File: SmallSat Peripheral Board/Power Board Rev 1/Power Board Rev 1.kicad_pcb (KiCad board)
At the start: 2 copper layers, 37 parts, among them U1 DMN3020UFDF, U2 BQ296202DSGR, U3 DMN3020UFDF, U4 BQ28Z620DRZR, U5 TPS62993QRYTRQ1, U6 TPS62993QRYTRQ1

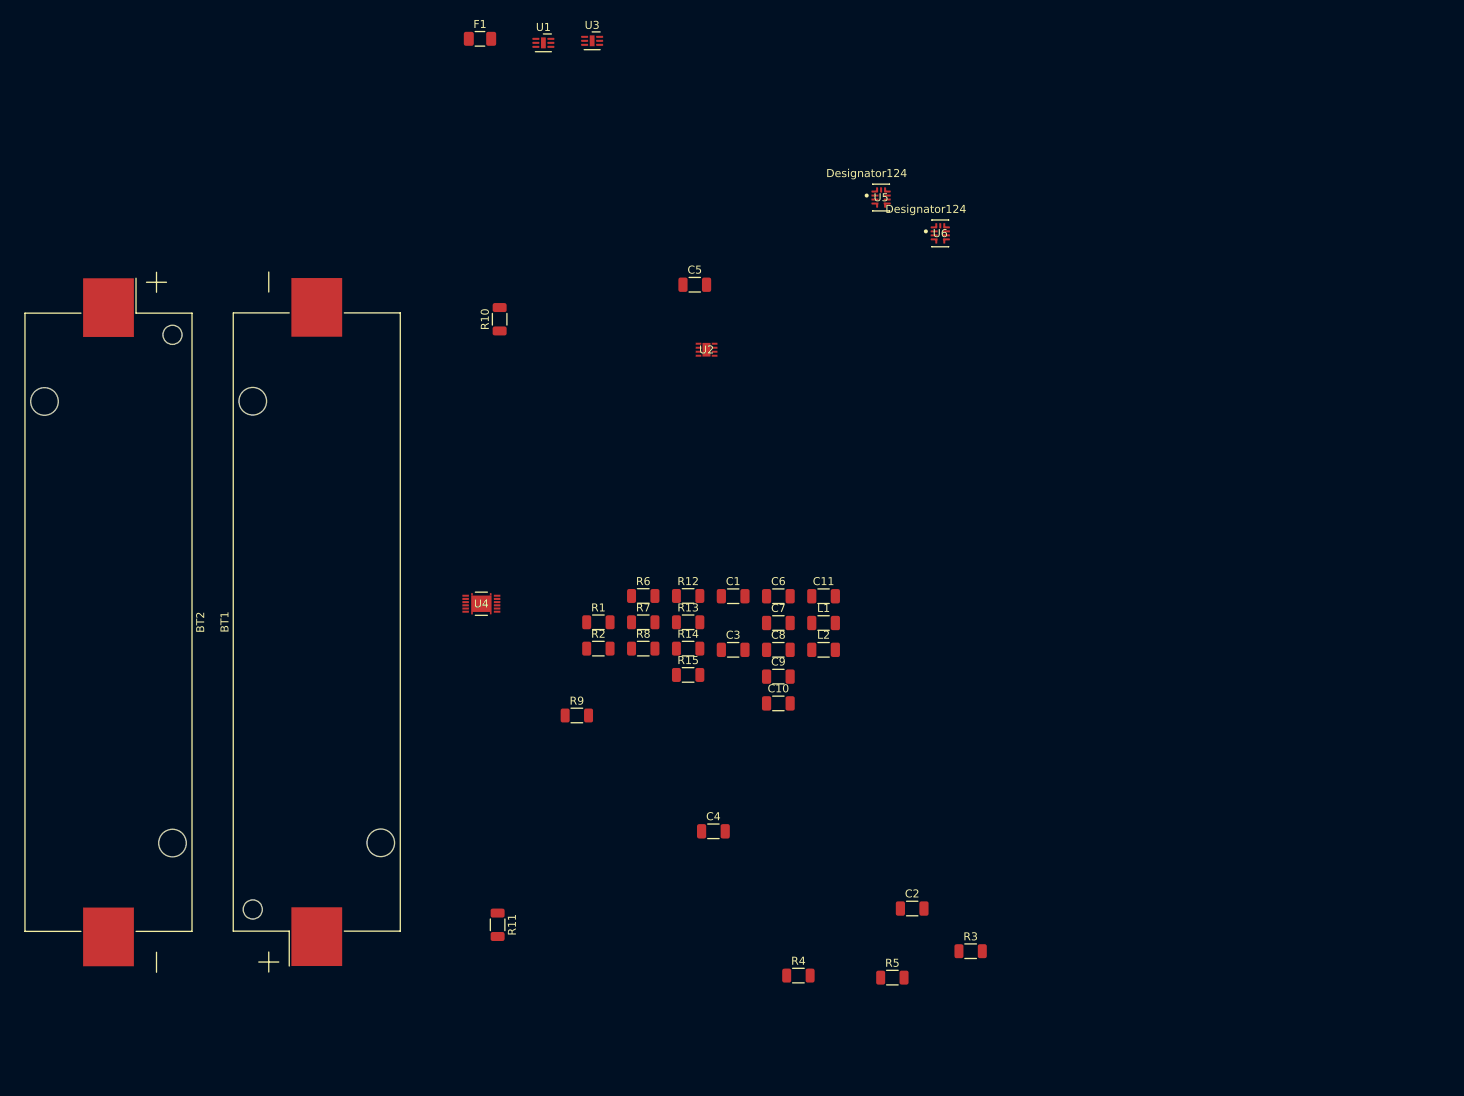
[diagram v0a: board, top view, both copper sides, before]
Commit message: Power Board Grouping
- Continuing to group parts
- Connectors figured out
- Filter circuit must be close to BQ298
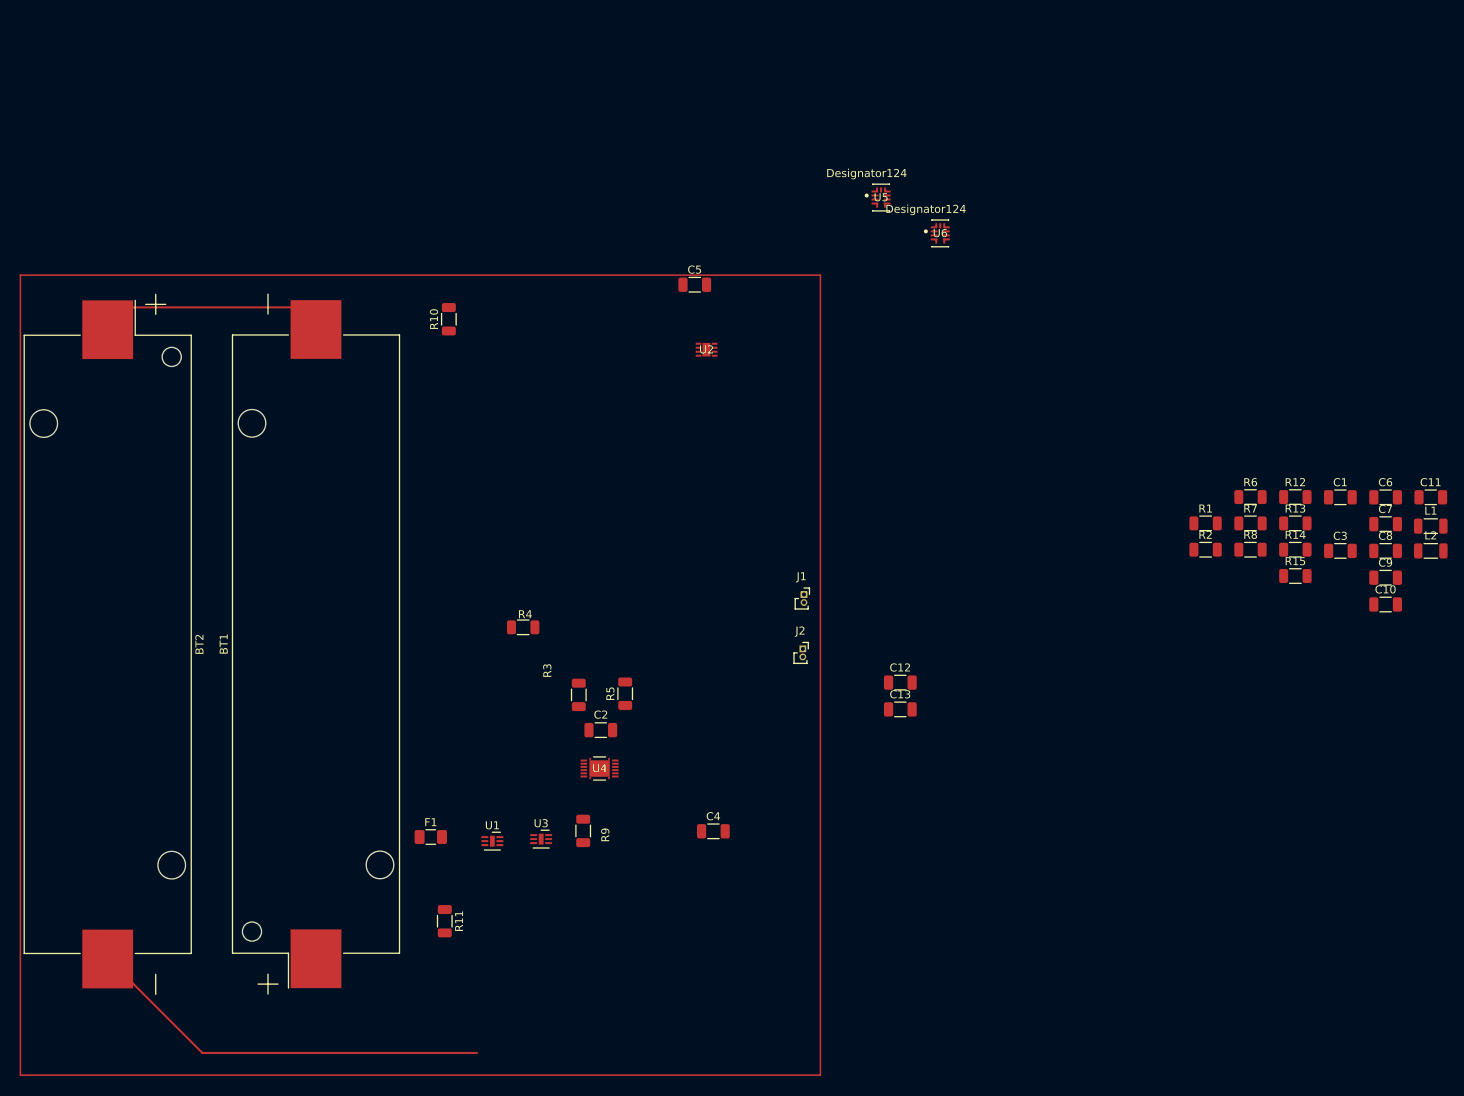
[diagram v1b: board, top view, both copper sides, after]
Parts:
- added C12: 0.1u, Capacitor_SMD:C_1206_3216Metric, F.Cu at (187.0, 108.4)
- added C13: 0.1u, Capacitor_SMD:C_1206_3216Metric, F.Cu at (187.0, 111.8)
- added J1: Conn_01x02_Pin, Connector_PinSocket_1.00mm:PinSocket_1x02_P1.00mm_Vertical, F.Cu at (174.9, 97.4)
- added J2: Conn_01x02_Pin, Connector_PinSocket_1.00mm:PinSocket_1x02_P1.00mm_Vertical, F.Cu at (174.8, 104.2)
- L1, L2: footprint Capacitor_SMD:C_1206_3216Metric -> Inductor_SMD:L_1206_3216Metric
- R3, R5: value 10m -> 100
- moved U1 100.0 mm to (136.0, 128.2)
- moved U3 100.0 mm to (142.1, 128.0)
- moved F1 100.0 mm to (128.3, 127.7)
- moved C1 76.9 mm to (242.0, 85.2)
- moved C10 76.9 mm to (247.7, 98.6)
- moved C11 76.9 mm to (253.3, 85.2)
- moved C3 76.9 mm to (242.0, 91.9)
- moved C6 76.9 mm to (247.7, 85.2)
- moved C7 76.9 mm to (247.7, 88.6)
- moved C8 76.9 mm to (247.7, 91.9)
- moved C9 76.9 mm to (247.7, 95.3)
- moved L2 76.9 mm to (253.3, 91.9)
- moved R1 76.9 mm to (225.2, 88.5)
- moved R12 76.9 mm to (236.4, 85.2)
- moved R13 76.9 mm to (236.4, 88.5)
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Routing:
- net GND: track 0.00 -> 54.1 mm
- net /B1+: track 0.00 -> 26.0 mm
- net /B2+: track 0.00 -> 6.14 mm

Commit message: Current Line Outline Complete
- OV/UV protection IC wired
- fuel gauge not wired
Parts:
- R2: value 1k -> 100
- moved R10 136.4 mm to (248.3, 131.8)
- moved C2 87.2 mm to (235.2, 131.2)
- moved C4 87.2 mm to (249.2, 143.8)
- moved R11 87.2 mm to (215.6, 155.1)
- moved R3 87.2 mm to (232.4, 126.8)
- moved R4 87.2 mm to (225.4, 118.3)
- moved R5 87.2 mm to (238.2, 126.7)
- moved R9 87.2 mm to (232.9, 143.8)
- moved L2 85.6 mm to (168.8, 105.0), turned to 180 degrees
- moved L1 84.8 mm to (169.0, 97.8), turned to 180 degrees
- moved R6 82.9 mm to (153.4, 115.0)
- moved C1 81.4 mm to (169.5, 122.3), turned to 90 degrees
- moved C3 75.3 mm to (173.1, 122.2), turned to -90 degrees
- moved R7 73.0 mm to (161.3, 111.0), turned to 90 degrees
- moved R2 72.8 mm to (163.6, 130.7), turned to -90 degrees
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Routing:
- net /B1+: track 26.0 -> 92.9 mm, vias 0 -> 2
- net /B2+: track 6.14 -> 61.0 mm
- net GND: track 54.1 -> 3.16 mm
- net /PACK+: track 0.00 -> 24.8 mm
- net Net-(U2-V1): track 0.00 -> 12.4 mm
- net Net-(U2-V2): track 0.00 -> 10.9 mm
- net Net-(U3-G): track 0.00 -> 10.6 mm, vias 0 -> 1
- net Net-(U1-D): track 0.00 -> 9.46 mm
- net /OUT: track 0.00 -> 7.42 mm
- net /BATT+: track 0.00 -> 6.65 mm
- net Net-(U2-VDD): track 0.00 -> 5.60 mm
- net /5V: track 0.00 -> 4.68 mm
- net /3.3V: track 0.00 -> 4.64 mm
- net Net-(U5-SW): track 0.00 -> 3.70 mm
- net Net-(U6-SW): track 0.00 -> 3.54 mm

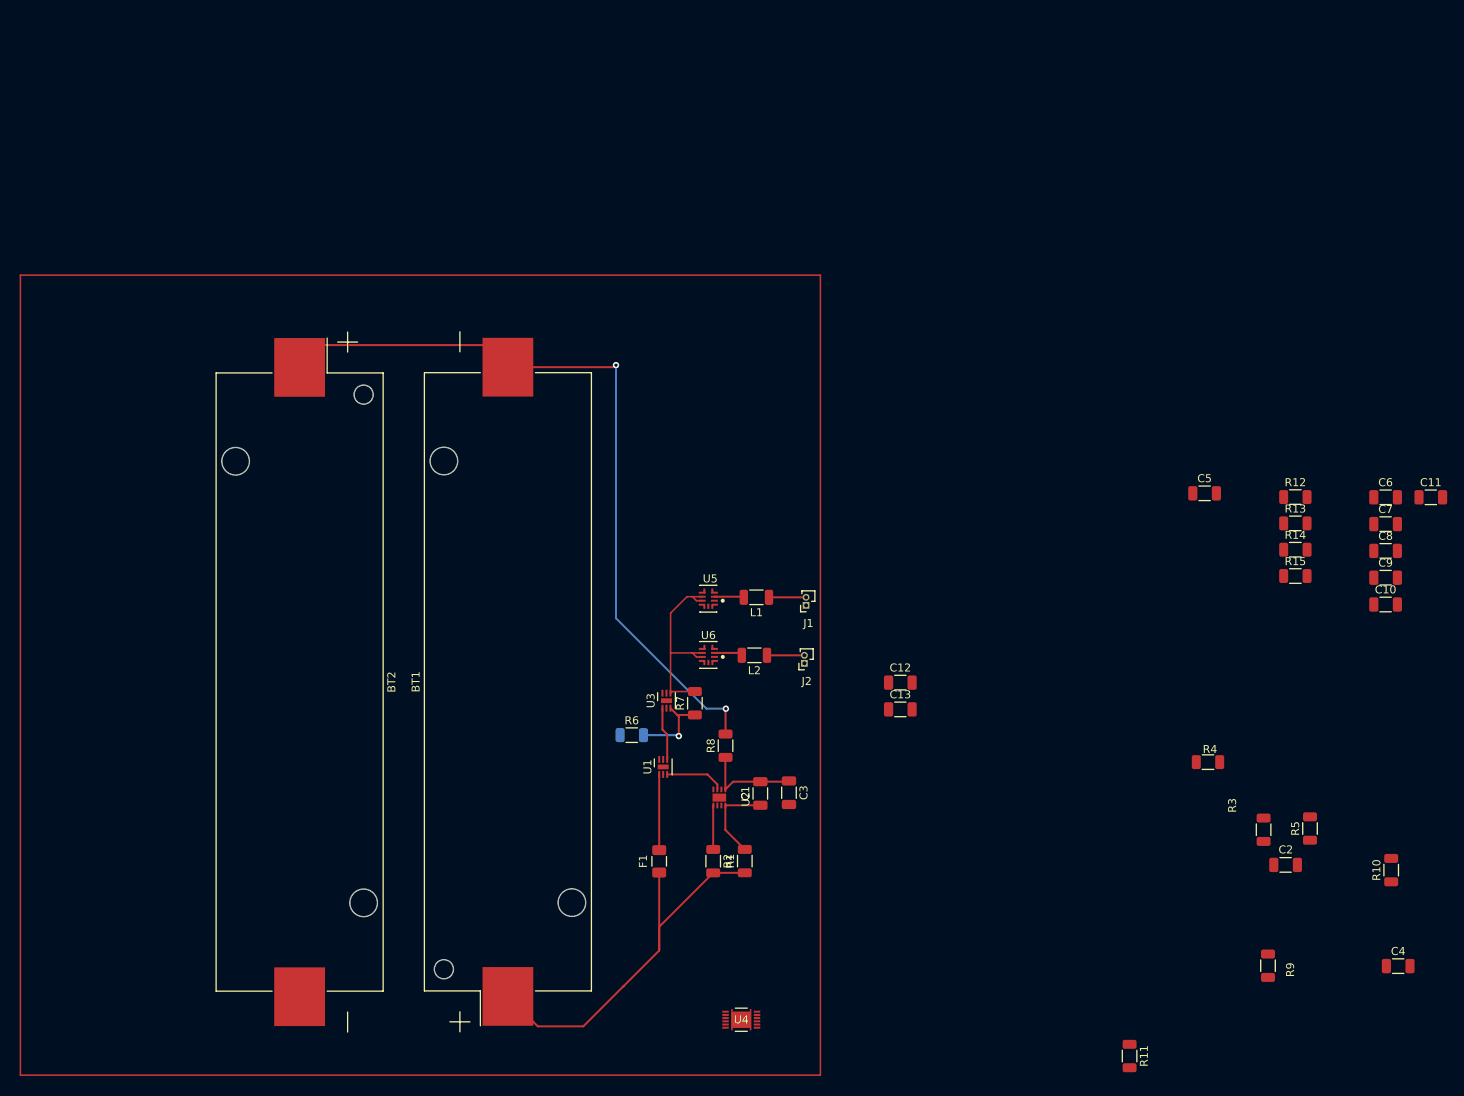
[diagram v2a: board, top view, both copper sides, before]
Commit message: Power Board Connections Complete
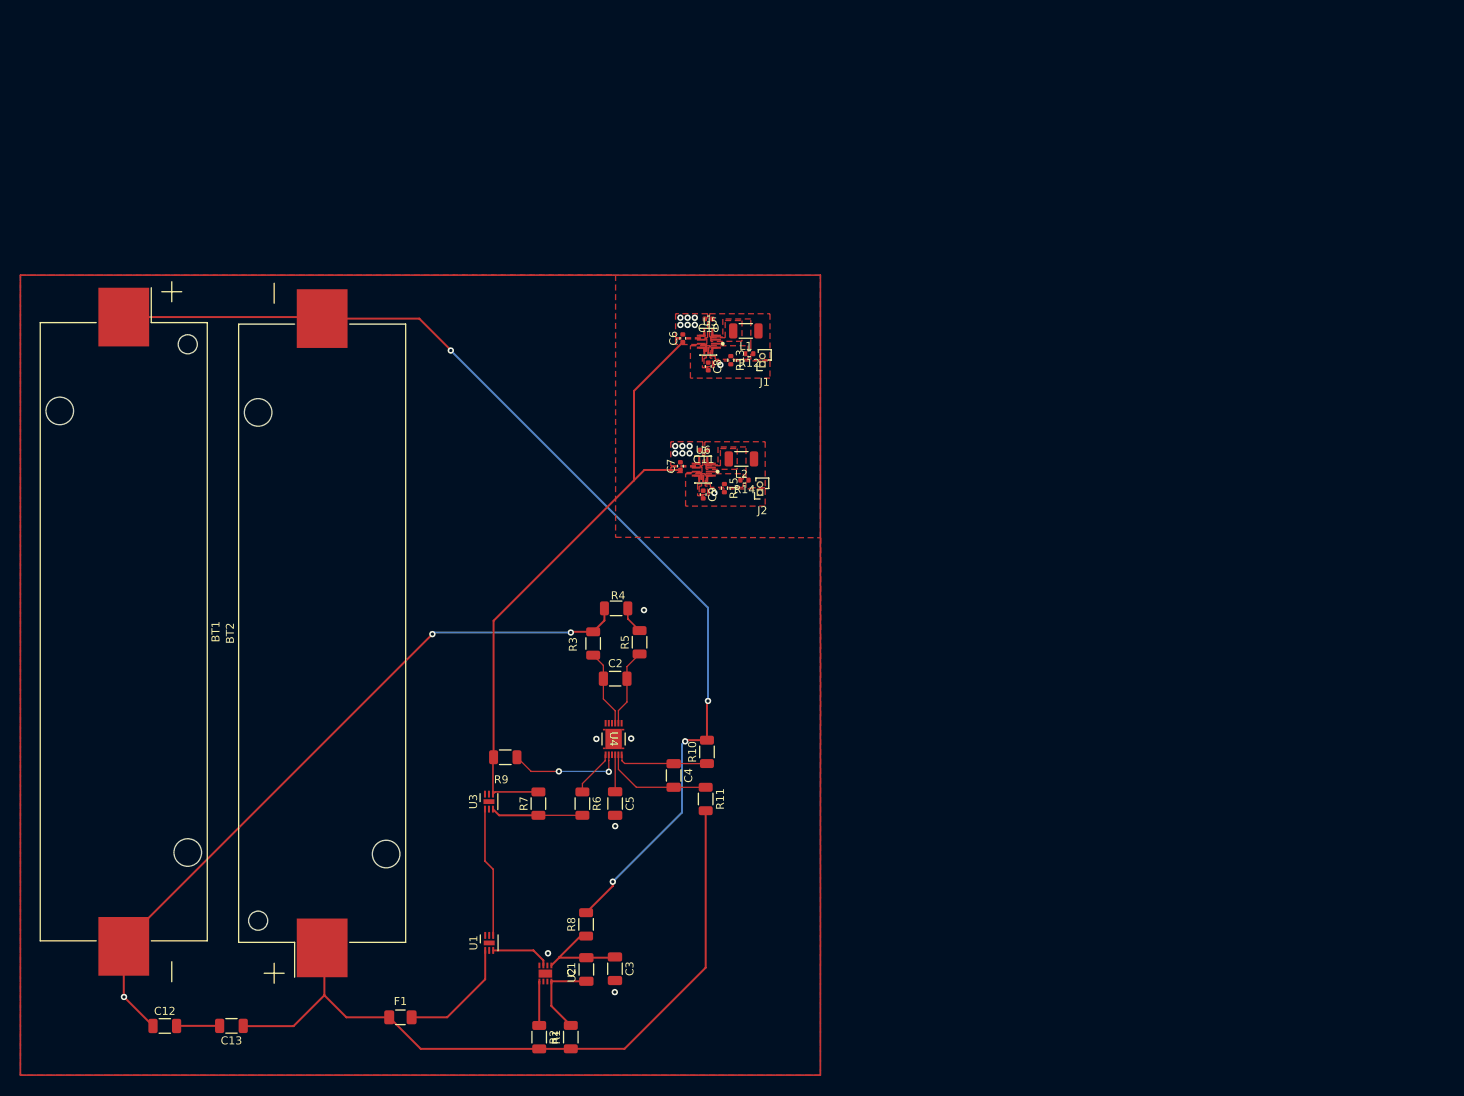
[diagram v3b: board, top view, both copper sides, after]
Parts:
- C10, C11, C6, C7, C8, C9: footprint Capacitor_SMD:C_1206_3216Metric -> Capacitor_SMD:C_0402_1005Metric
- R12, R13, R14, R15: footprint Resistor_SMD:R_1206_3216Metric -> Resistor_SMD:R_0402_1005Metric
- moved C12 101.5 mm to (95.0, 151.3)
- moved R9 98.8 mm to (137.6, 117.7), turned to 180 degrees
- moved C4 93.6 mm to (158.7, 120.0), turned to -90 degrees
- moved C13 92.5 mm to (103.4, 151.3), turned to 180 degrees
- moved C10 91.8 mm to (163.0, 63.0), turned to 180 degrees
- moved C11 91.1 mm to (162.4, 79.3), turned to 180 degrees
- moved C6 90.1 mm to (159.8, 65.4), turned to 90 degrees
- moved C7 88.4 mm to (159.5, 81.3), turned to 90 degrees
- moved C8 87.8 mm to (163.0, 68.9), turned to -90 degrees
- moved C2 87.0 mm to (151.3, 107.9)
- moved R3 87.0 mm to (148.6, 103.5)
- moved R5 87.0 mm to (154.4, 103.4)
- moved R10 86.8 mm to (162.8, 117.1)
- moved C9 85.9 mm to (162.3, 84.9), turned to -90 degrees
- moved C5 83.3 mm to (151.3, 123.5), turned to -90 degrees
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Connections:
- net Net-(U5-FB_VSET) renamed /FB_VSET_3V3
- net Net-(U5-SS_TR) renamed /SS_TR_3V3
- net Net-(U5-SW) renamed /SW_3V3
- net Net-(U6-FB_VSET) renamed /FB_VSET_5V
- net Net-(U6-SS_TR) renamed /SS_TR_5V
- net Net-(U6-SW) renamed /SW_5V
- BT1 pad 1: /B2+ -> /B1+
- BT1 pad 2: /B1+ -> /BATT-
- BT2 pad 1: /B1+ -> /B2+
- BT2 pad 2: GND -> /B1+
- R3 pad 2: GND -> /BATT-
- R4 pad 1: GND -> /BATT-
- R4 pad 2: /PACK- -> GND
- R5 pad 2: /PACK- -> GND
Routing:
- net /BATT-: track 0.00 -> 78.5 mm, vias 0 -> 2
- net /PACK+: track 24.8 -> 78.6 mm
- net /B1+: track 92.9 -> 134.1 mm, vias 2 -> 4
- net /B2+: track 61.0 -> 91.9 mm
- net GND: track 3.16 -> 18.0 mm, vias 0 -> 21
- net Net-(U4-PACK): track 0.00 -> 14.4 mm, vias 0 -> 2
- net Net-(U4-VC2): track 0.00 -> 13.7 mm
- net Net-(U4-VC1): track 0.00 -> 11.5 mm
- net /SRN: track 0.00 -> 9.75 mm
- net /SRP: track 0.00 -> 9.65 mm
- net /BATT+: track 6.65 -> 16.2 mm
- net /DSG: track 0.00 -> 5.97 mm
- net Net-(C12-Pad2): track 0.00 -> 5.40 mm
- net Net-(U1-D): track 9.46 -> 14.8 mm
- net /5V: track 4.68 -> 0.00 mm
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- added copper zone on F.Cu, net /3.3V
- added copper zone on F.Cu, net /5V
- added copper zone on F.Cu, net /FB_VSET_3V3
- added copper zone on F.Cu, net /FB_VSET_5V
- added copper zone on F.Cu, net /PACK+
- added copper zone on F.Cu, net /SS_TR_3V3
- added copper zone on F.Cu, net /SS_TR_5V
- added copper zone on F.Cu, net /SW_3V3
- added copper zone on F.Cu, net /SW_5V
- added copper zone on B.Cu, net GND
- added copper zone on F.Cu, net GND
